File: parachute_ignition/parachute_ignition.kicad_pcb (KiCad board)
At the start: 2 copper layers, 29.2 x 27.9 mm, 9 parts, among them P1 CONN_01X02, Q1 IRF7413ZPBF, U1 4047

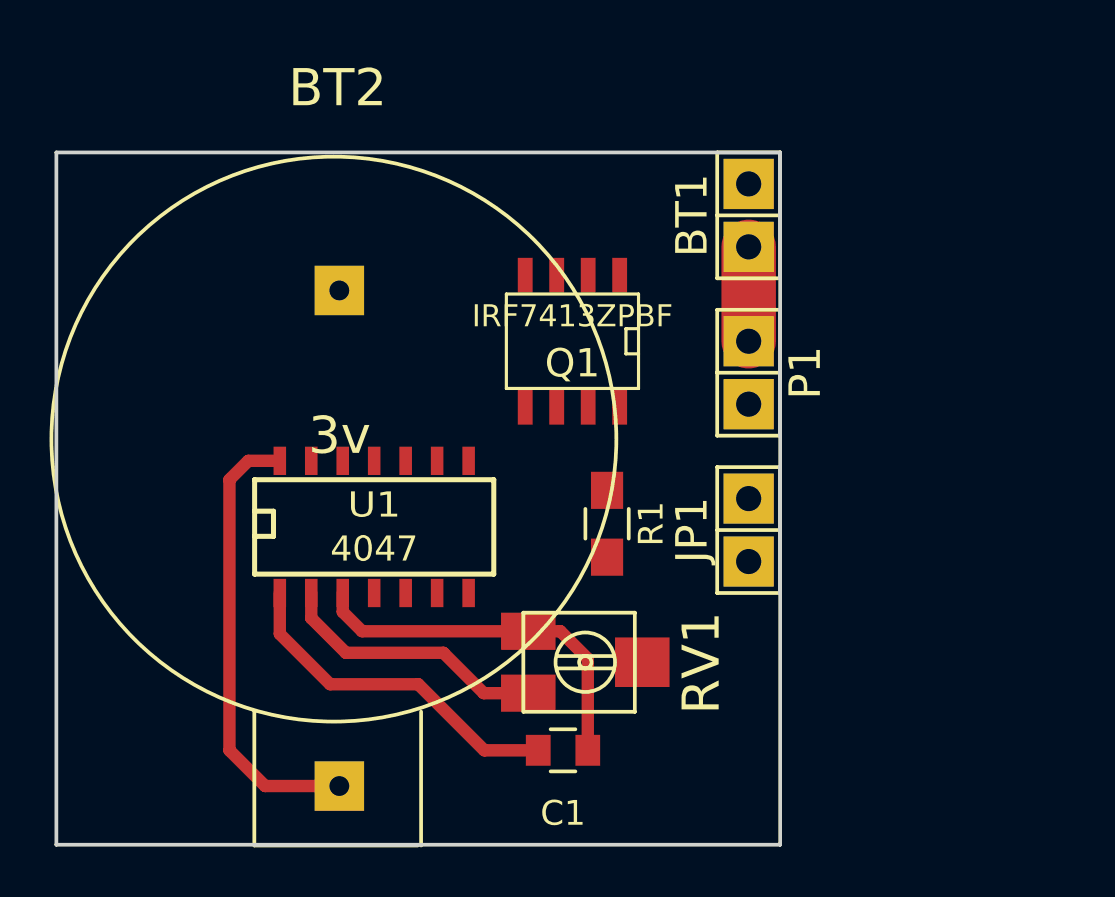
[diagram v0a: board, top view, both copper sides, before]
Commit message: prarachute ignition pcb added
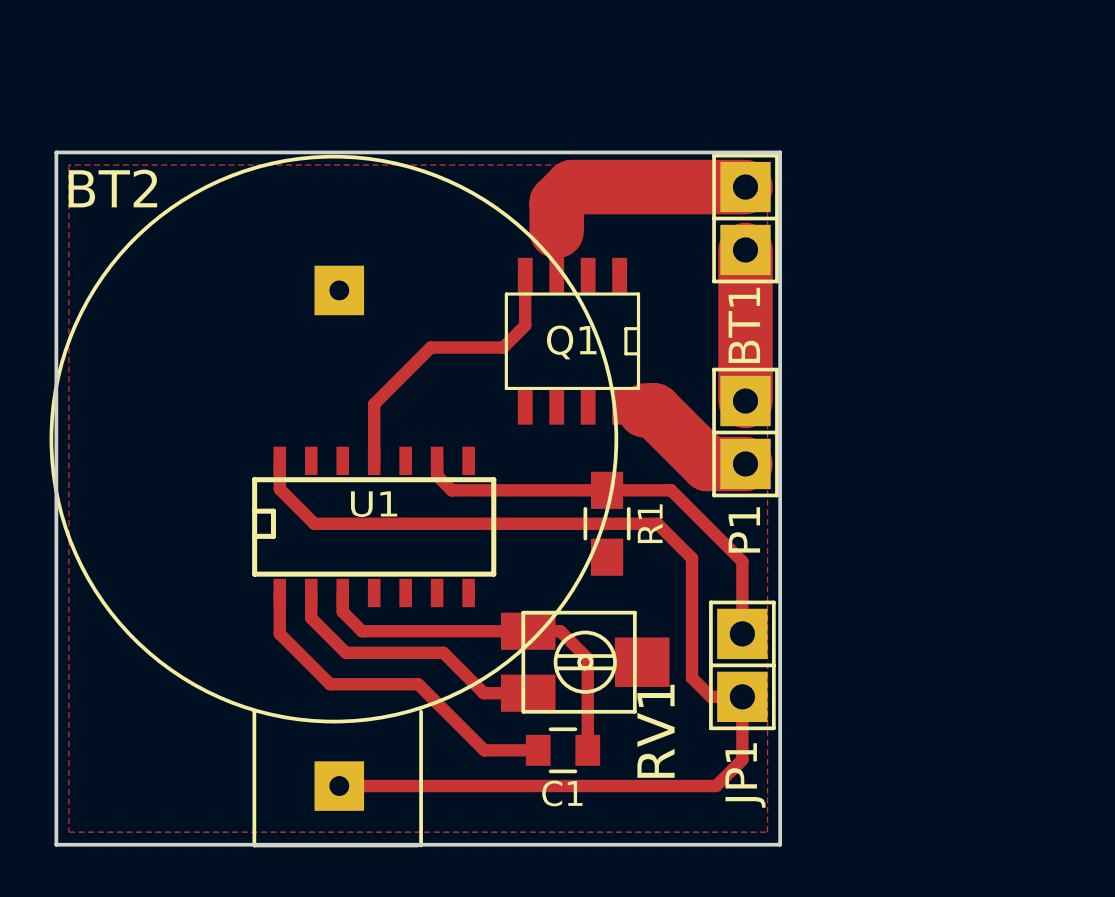
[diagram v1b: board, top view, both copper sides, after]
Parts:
- moved JP1 5.47 mm to (200.4, 100.7)
- moved P1 2.42 mm to (200.5, 91.3)
- moved BT1 0.18 mm to (200.5, 82.7)
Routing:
- net VCC: track 18.3 -> 45.4 mm
- net Net-(JP1-Pad2): track 0.47 -> 17.7 mm
- net Net-(Q1-Pad4): track 0.00 -> 11.7 mm
- net Net-(BT1-Pad2): track 0.00 -> 10.3 mm
- net Net-(P1-Pad2): track 0.00 -> 5.59 mm
- net Net-(BT1-Pad1): track 3.81 -> 6.10 mm
- added copper zone on F.Cu, net GND

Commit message: last improvments and pcbs
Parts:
- moved P1 1.52 mm to (200.5, 89.8)
- moved Q1 1.14 mm to (193.5, 86.5)
- moved BT1 0.76 mm to (200.5, 83.4)
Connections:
- Q1 pad 1: (no net) -> Net-(BT1-Pad2)
- Q1 pad 2: (no net) -> Net-(BT1-Pad2)
- Q1 pad 5: (no net) -> Net-(P1-Pad2)
- Q1 pad 6: (no net) -> Net-(P1-Pad2)
- Q1 pad 7: (no net) -> Net-(P1-Pad2)
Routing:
- net Net-(P1-Pad2): track 5.59 -> 16.7 mm
- net Net-(BT1-Pad1): track 6.10 -> 3.81 mm
- net Net-(BT1-Pad2): track 10.3 -> 12.3 mm
- net Net-(Q1-Pad4): track 11.7 -> 12.9 mm
